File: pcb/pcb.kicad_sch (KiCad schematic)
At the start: 232 parts

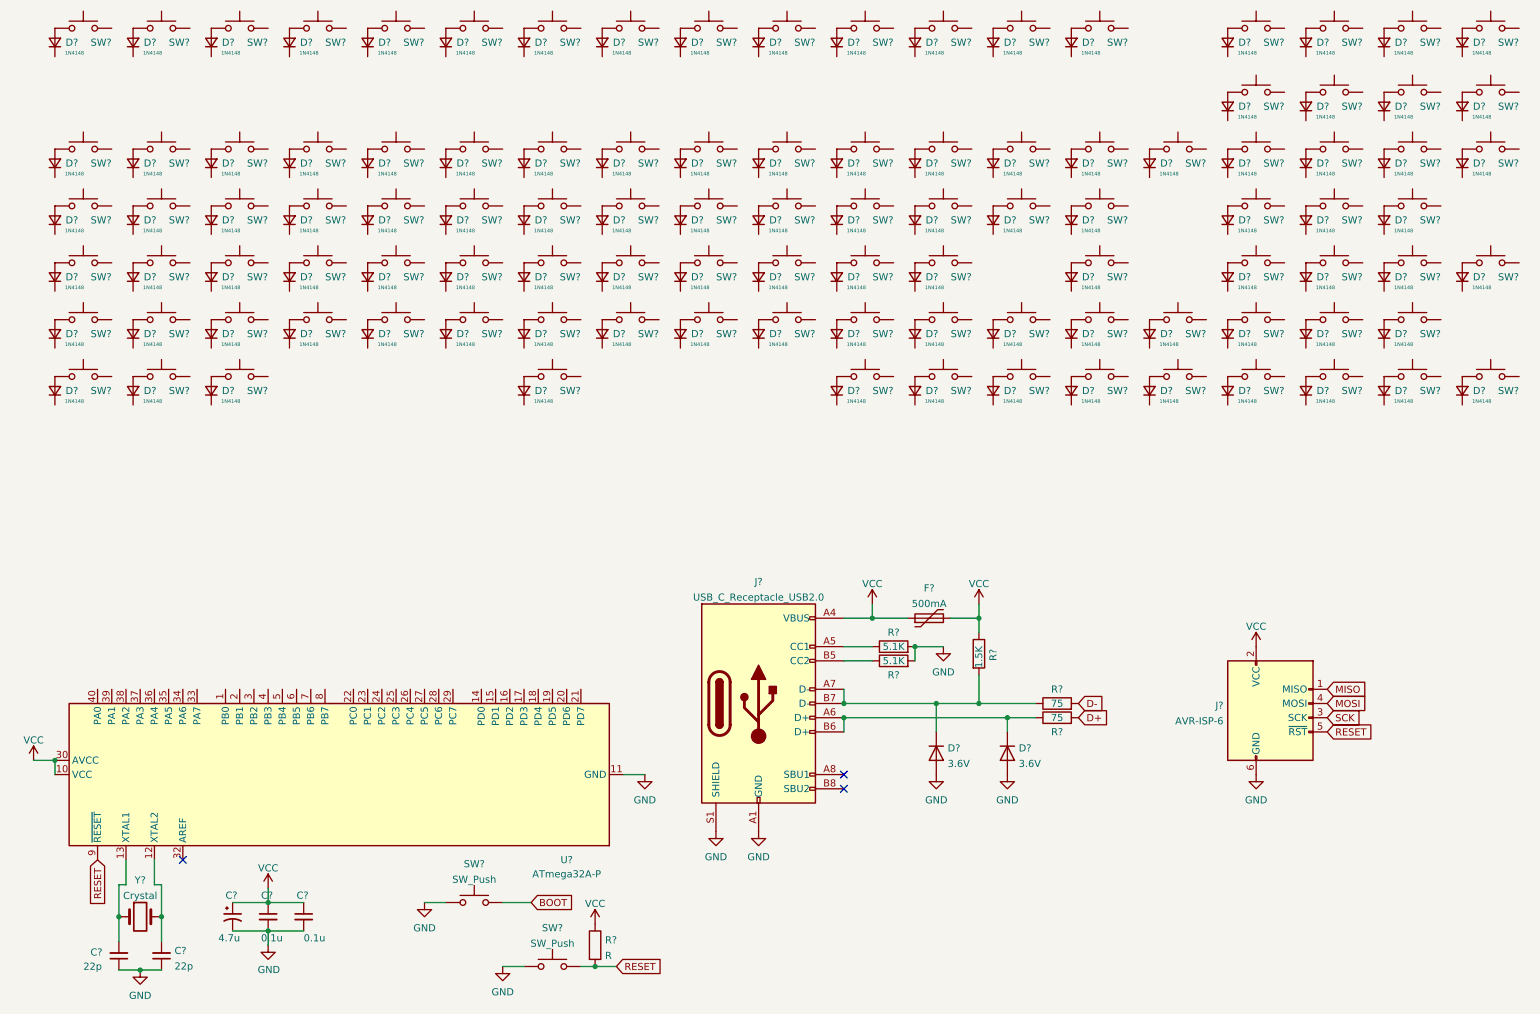
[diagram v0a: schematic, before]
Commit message: Wired duplex matrix
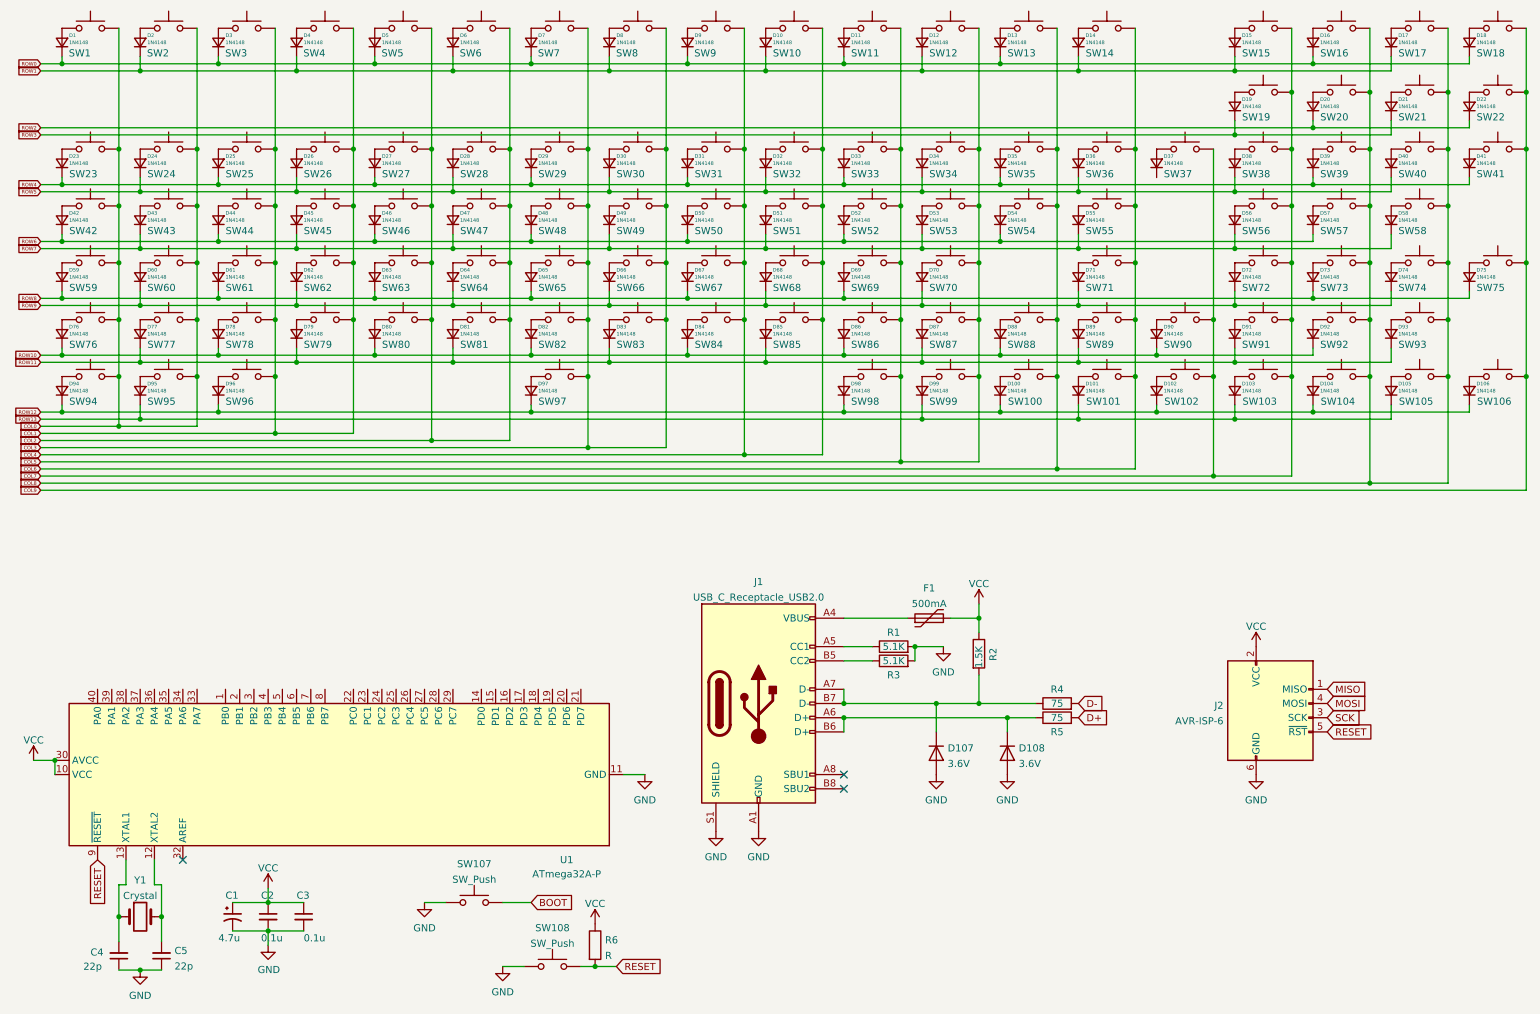
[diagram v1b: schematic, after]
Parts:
- gave numbers to parts that had none: 232
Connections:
- net VCC: no longer F1.1, J1.A4 (VBUS), J1.A9 (VBUS), J1.B4 (VBUS), J1.B9 (VBUS)
- net ROW3: now reaches D19.1 (K)
- net ROW3: now also D21.1 (K)
- net COL0: now reaches SW77.2
- net COL0: now also SW1.2, SW2.2, SW23.2, SW24.2, SW42.2, SW43.2, SW59.2, SW60.2, SW76.2, SW94.2, SW95.2
- net COL8: now reaches SW20.2
- net COL8: now also SW104.2, SW105.2, SW16.2, SW17.2, SW21.2, SW39.2, SW40.2, SW57.2, SW58.2, SW73.2, SW74.2, SW92.2, SW93.2
- net ROW9: now reaches D70.1 (K)
- net ROW9: now also D60.1 (K), D62.1 (K), D64.1 (K), D66.1 (K), D68.1 (K), D71.1 (K), D72.1 (K), D74.1 (K)
- net ROW1: now reaches D10.1 (K)
- net ROW1: now also D12.1 (K), D14.1 (K), D15.1 (K), D17.1 (K), D2.1 (K), D4.1 (K), D6.1 (K), D8.1 (K)
- net ROW8: now reaches D65.1 (K)
- net ROW8: now also D59.1 (K), D61.1 (K), D63.1 (K), D67.1 (K), D69.1 (K), D73.1 (K), D75.1 (K)
- net ROW7: now reaches D43.1 (K)
- net ROW7: now also D45.1 (K), D47.1 (K), D49.1 (K), D51.1 (K), D53.1 (K), D55.1 (K), D56.1 (K), D58.1 (K)
- net COL7: now reaches SW38.2
- net COL7: now also SW102.2, SW103.2, SW15.2, SW19.2, SW37.2, SW56.2, SW72.2, SW90.2, SW91.2
- net ROW12: now reaches D98.1 (K)
- net ROW12: now also D100.1 (K), D102.1 (K), D104.1 (K), D106.1 (K), D94.1 (K), D96.1 (K), D97.1 (K)
- net ROW5: now reaches D34.1 (K)
- net ROW5: now also D24.1 (K), D26.1 (K), D28.1 (K), D30.1 (K), D32.1 (K), D36.1 (K), D38.1 (K), D40.1 (K)
- net COL1: now reaches SW4.2
- net COL1: now also SW25.2, SW26.2, SW3.2, SW44.2, SW45.2, SW61.2, SW62.2, SW78.2, SW79.2, SW96.2
- net COL3: now reaches SW82.2
- net COL3: now also SW29.2, SW30.2, SW48.2, SW49.2, SW65.2, SW66.2, SW7.2, SW8.2, SW83.2, SW97.2
- net ROW11: now reaches D91.1 (K)
- net ROW11: now also D77.1 (K), D79.1 (K), D81.1 (K), D83.1 (K), D85.1 (K), D87.1 (K), D89.1 (K), D93.1 (K)
- net COL5: now reaches SW52.2
- net COL5: now also SW11.2, SW12.2, SW33.2, SW34.2, SW53.2, SW69.2, SW70.2, SW86.2, SW87.2, SW98.2, SW99.2
- net COL4: now reaches SW84.2
- net COL4: now also SW10.2, SW31.2, SW32.2, SW50.2, SW51.2, SW67.2, SW68.2, SW85.2, SW9.2
- net ROW0: now reaches D16.1 (K)
- net ROW0: now also D1.1 (K), D11.1 (K), D13.1 (K), D18.1 (K), D3.1 (K), D5.1 (K), D7.1 (K), D9.1 (K)
- net COL2: now reaches SW47.2
- net COL2: now also SW27.2, SW28.2, SW46.2, SW5.2, SW6.2, SW63.2, SW64.2, SW80.2, SW81.2
- net ROW10: now reaches D76.1 (K)
- net ROW10: now also D78.1 (K), D80.1 (K), D82.1 (K), D84.1 (K), D86.1 (K), D88.1 (K), D90.1 (K), D92.1 (K)
- net ROW4: now reaches D27.1 (K)
- net ROW4: now also D23.1 (K), D25.1 (K), D29.1 (K), D31.1 (K), D33.1 (K), D35.1 (K), D39.1 (K), D41.1 (K)
- net ROW13: now reaches D105.1 (K)
- net ROW13: now also D101.1 (K), D103.1 (K), D95.1 (K), D99.1 (K)
- net ROW2: now reaches D20.1 (K)
- net ROW2: now also D22.1 (K)
- net COL6: now reaches SW36.2
- net COL6: now also SW100.2, SW101.2, SW13.2, SW14.2, SW35.2, SW54.2, SW55.2, SW71.2, SW88.2, SW89.2
- net ROW6: now reaches D44.1 (K)
- net ROW6: now also D42.1 (K), D46.1 (K), D48.1 (K), D50.1 (K), D52.1 (K), D54.1 (K), D57.1 (K)
- net COL9: now reaches SW106.2
- net COL9: now also SW18.2, SW22.2, SW41.2, SW75.2
- new net: F1.1, J1.A4 (VBUS), J1.A9 (VBUS), J1.B4 (VBUS), J1.B9 (VBUS)
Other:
- moved on the sheet: D1, D10, D100, D101, D102, D103, D104, D105, D106, D11, D12, D13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

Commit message: Redid wiring on schematic because I hate myself
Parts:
- added SW107: 1U CTRL, MX_Only:MXOnly-1U-NoLED, symbol Switch:SW_Push
- added SW108, SW109, SW110, SW111, SW112, SW113: 1U, MX_Only:MXOnly-1U-NoLED, symbol Switch:SW_Push
- added SW114, SW119: 1.5U CTRL, MX_Only:MXOnly-1.5U-NoLED, symbol Switch:SW_Push
- added SW115: 1U GUI, MX_Only:MXOnly-1U-NoLED, symbol Switch:SW_Push
- added SW116, SW118: 1.5U ALT, MX_Only:MXOnly-1.5U-NoLED, symbol Switch:SW_Push
- added SW117: 7U SPACE, MX_Only:MXOnly-7U-NoLED, symbol Switch:SW_Push
- added SW120: 1.5U GUI, MX_Only:MXOnly-1.5U-NoLED, symbol Switch:SW_Push
- added SW121: 6U SPACE, MX_Only:MXOnly-6U-NoLED, symbol Switch:SW_Push
- C1: footprint cftkb:CP_Radial_D4.0mm_P1.50mm -> Capacitor_THT:CP_Radial_D4.0mm_P1.50mm
- C2, C3: footprint cftkb:C_Disc_D4.3mm_W1.9mm_P5.00mm -> Capacitor_THT:C_Disc_D4.3mm_W1.9mm_P5.00mm
- C4, C5: footprint (none) -> Capacitor_THT:C_Disc_D3.0mm_W1.6mm_P2.50mm
- D1, D10, D100, D101, D102, D103, D104, D105, D106, D11, D12, D13, D14, D15, D16, D17, D18, D19, D2, D20, D21, D22, D23, D24, D25, D26, D27, D28, D29, D3, D30, D31, D32, D33, D34, D35, D36, D37, D38, D39, D4, D40, D41, D42, D43, D44, D45, D46, D47, D48, D49, D5, D50, D51, D52, D53, D54, D55, D56, D57, D58, D59, D6, D60, D61, D62, D63, D64, D65, D66, D67, D68, D69, D7, D70, D71, D72, D73, D74, D75, D76, D77, D78, D79, D8, D80, D81, D82, D83, D84, D85, D86, D87, D88, D89, D9, D90, D91, D92, D93, D94, D95, D96, D97, D98, D99: footprint (none) -> Diode_THT:D_DO-35_SOD27_P7.62mm_Horizontal
- D107, D108: footprint (none) -> Diode_THT:D_DO-41_SOD81_P7.62mm_Horizontal
- F1: footprint (none) -> Fuse:Fuse_BelFuse_0ZRE0025FF_L9.6mm_W3.8mm
- J1: footprint (none) -> Connector_USB:USB_C_Receptacle_GCT_USB4085
- J2: footprint (none) -> Connector_PinHeader_2.54mm:PinHeader_2x03_P2.54mm_Vertical
- R1, R2, R3, R4, R5: footprint (none) -> Resistor_THT:R_Axial_DIN0204_L3.6mm_D1.6mm_P7.62mm_Horizontal
- R6: value R -> 10k; footprint (none) -> Resistor_THT:R_Axial_DIN0204_L3.6mm_D1.6mm_P7.62mm_Horizontal
- SW1, SW10, SW11, SW12, SW13, SW14, SW15, SW16, SW17, SW18, SW19, SW2, SW20, SW21, SW22, SW23, SW24, SW25, SW26, SW27, SW28, SW29, SW3, SW30, SW31, SW32, SW33, SW34, SW35, SW36, SW37, SW38, SW39, SW4, SW40, SW42, SW44, SW45, SW46, SW47, SW48, SW49, SW5, SW50, SW51, SW52, SW53, SW54, SW56, SW57, SW58, SW59, SW6, SW63, SW64, SW65, SW66, SW67, SW68, SW69, SW7, SW70, SW71, SW72, SW73, SW75, SW76, SW77, SW78, SW8, SW82, SW83, SW84, SW85, SW86, SW87, SW88, SW89, SW9, SW90, SW91, SW92, SW94, SW95, SW96, SW97, SW98: value SW_Push -> 1U; footprint (none) -> MX_Only:MXOnly-1U-NoLED
- SW100, SW41, SW60, SW74: value SW_Push -> 2U; footprint (none) -> MX_Only:MXOnly-2U-NoLED
- SW101: value SW_Push -> 1.25U CTRL; footprint (none) -> MX_Only:MXOnly-1.25U-NoLED
- SW102: value SW_Push -> 1.25U GUI; footprint (none) -> MX_Only:MXOnly-1.25U-NoLED
- SW103: value SW_Push -> 1.25U ALT; footprint (none) -> MX_Only:MXOnly-1.25U-NoLED
- SW104: value SW_Push -> 6.25u SPACE; footprint (none) -> MX_Only:MXOnly-6.25U-NoLED
- SW105: value SW_Push -> 1U ALT; footprint (none) -> MX_Only:MXOnly-1U-NoLED
- SW106: value SW_Push -> 1U GUI; footprint (none) -> MX_Only:MXOnly-1U-NoLED
- SW122: renamed from SW107; footprint (none) -> Button_Switch_THT:SW_PUSH_6mm_H5mm
- SW123: renamed from SW108; footprint (none) -> Button_Switch_THT:SW_PUSH_6mm_H5mm
- SW43, SW55: value SW_Push -> 1.5U; footprint (none) -> MX_Only:MXOnly-1.5U-NoLED
- SW61: value SW_Push -> ISO ENTER; footprint (none) -> MX_Only:MXOnly-ISO-NoLED
- SW62: value SW_Push -> CAPSLOCK; footprint (none) -> MX_Only:MXOnly-1.75U-NoLED
- SW79: value SW_Push -> STEPPED; footprint (none) -> MX_Only:MXOnly-1.25U-NoLED
- SW80: value SW_Push -> ISO 1U; footprint (none) -> MX_Only:MXOnly-1U-NoLED
- SW81: value SW_Push -> 2.25U; footprint (none) -> MX_Only:MXOnly-2.25U-NoLED
- SW93: value SW_Push -> 1.75U SHIFT; footprint (none) -> MX_Only:MXOnly-1.75U-NoLED
- SW99: value SW_Push -> ISO SHIFT; footprint (none) -> MX_Only:MXOnly-1.25U-NoLED
- Y1: footprint (none) -> Crystal:Crystal_HC49-4H_Vertical
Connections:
- net COL0: no longer SW1.2, SW2.2, SW23.2, SW24.2, SW42.2, SW43.2, SW59.2, SW60.2, SW76.2, SW77.2, SW94.2, SW95.2
- net COL1: no longer SW25.2, SW26.2, SW3.2, SW4.2, SW44.2, SW45.2, SW61.2, SW62.2, SW78.2, SW79.2, SW96.2
- net COL2: no longer SW27.2, SW28.2, SW46.2, SW47.2, SW5.2, SW6.2, SW63.2, SW64.2, SW80.2, SW81.2
- net COL3: no longer SW29.2, SW30.2, SW48.2, SW49.2, SW65.2, SW66.2, SW7.2, SW8.2, SW82.2, SW83.2, SW97.2
- net COL4: no longer SW10.2, SW31.2, SW32.2, SW50.2, SW51.2, SW67.2, SW68.2, SW84.2, SW85.2, SW9.2
- net COL5: no longer SW11.2, SW12.2, SW33.2, SW34.2, SW52.2, SW53.2, SW69.2, SW70.2, SW86.2, SW87.2, SW98.2, SW99.2
- net COL6: no longer SW100.2, SW101.2, SW13.2, SW14.2, SW35.2, SW36.2, SW54.2, SW55.2, SW71.2, SW88.2, SW89.2
- net COL7: no longer SW102.2, SW103.2, SW15.2, SW19.2, SW37.2, SW38.2, SW56.2, SW72.2, SW90.2, SW91.2
- net COL8: no longer SW104.2, SW105.2, SW16.2, SW17.2, SW20.2, SW21.2, SW39.2, SW40.2, SW57.2, SW58.2, SW73.2, SW74.2, SW92.2, SW93.2
- net COL9: no longer SW106.2, SW18.2, SW22.2, SW41.2, SW75.2
- net ROW0: no longer D1.1 (K), D11.1 (K), D13.1 (K), D16.1 (K), D18.1 (K), D3.1 (K), D5.1 (K), D7.1 (K), D9.1 (K)
- net ROW1: no longer D10.1 (K), D12.1 (K), D14.1 (K), D15.1 (K), D17.1 (K), D2.1 (K), D4.1 (K), D6.1 (K), D8.1 (K)
- net ROW10: no longer D76.1 (K), D78.1 (K), D80.1 (K), D82.1 (K), D84.1 (K), D86.1 (K), D88.1 (K), D90.1 (K), D92.1 (K)
- net ROW11: no longer D77.1 (K), D79.1 (K), D81.1 (K), D83.1 (K), D85.1 (K), D87.1 (K), D89.1 (K), D91.1 (K), D93.1 (K)
- net ROW12: no longer D100.1 (K), D102.1 (K), D104.1 (K), D106.1 (K), D94.1 (K), D96.1 (K), D97.1 (K), D98.1 (K)
- net ROW13: no longer D101.1 (K), D103.1 (K), D105.1 (K), D95.1 (K), D99.1 (K)
- net ROW2: no longer D20.1 (K), D22.1 (K)
- net ROW3: no longer D19.1 (K), D21.1 (K)
- net ROW4: no longer D23.1 (K), D25.1 (K), D27.1 (K), D29.1 (K), D31.1 (K), D33.1 (K), D35.1 (K), D39.1 (K), D41.1 (K)
- net ROW5: no longer D24.1 (K), D26.1 (K), D28.1 (K), D30.1 (K), D32.1 (K), D34.1 (K), D36.1 (K), D38.1 (K), D40.1 (K)
- net ROW6: no longer D42.1 (K), D44.1 (K), D46.1 (K), D48.1 (K), D50.1 (K), D52.1 (K), D54.1 (K), D57.1 (K)
- net ROW7: no longer D43.1 (K), D45.1 (K), D47.1 (K), D49.1 (K), D51.1 (K), D53.1 (K), D55.1 (K), D56.1 (K), D58.1 (K)
- net ROW8: no longer D59.1 (K), D61.1 (K), D63.1 (K), D65.1 (K), D67.1 (K), D69.1 (K), D73.1 (K), D75.1 (K)
- net ROW9: no longer D60.1 (K), D62.1 (K), D64.1 (K), D66.1 (K), D68.1 (K), D70.1 (K), D71.1 (K), D72.1 (K), D74.1 (K)
- net at D77.2 (A): now also SW82.1; no longer SW77.1
- net at SW70.1: now also D67.2 (A); no longer D70.2 (A)
- net at SW65.1: now also D62.2 (A); no longer D65.2 (A)
- net at D43.2 (A): now also SW44.1; no longer SW43.1
- net at SW98.1: now also D93.2 (A), SW100.1; no longer D98.2 (A)
- net at D95.2 (A): now also SW102.1, SW115.1, SW120.1; no longer SW95.1
- net at SW74.1: now also D71.2 (A), SW61.1; no longer D74.2 (A)
- net at D82.2 (A): now also SW87.1; no longer SW82.1
- net at D45.2 (A): now also SW46.1; no longer SW45.1
- net at D91.2 (A): now also SW96.1; no longer SW91.1
- net at SW66.1: now also D63.2 (A); no longer D66.2 (A)
- net at D56.2 (A): now also SW57.1; no longer SW56.1
- net at SW52.1: now also D51.2 (A); no longer D52.2 (A)
- net at SW84.1: now also D79.2 (A); no longer D84.2 (A)
- net at SW92.1: now also D87.2 (A); no longer D92.2 (A)
- net at SW79.1: now also D59.2 (A), SW62.1; no longer D79.2 (A)
- net at SW94.1: now also D89.2 (A); no longer D94.2 (A)
- net at D69.2 (A): now also SW72.1; no longer SW69.1
- net at SW47.1: now also D46.2 (A); no longer D47.2 (A)
- net at D76.2 (A): now also SW81.1, SW99.1; no longer SW76.1
- net at SW60.1: now also D58.2 (A), SW59.1; no longer D60.2 (A)
- net at D96.2 (A): now also SW103.1, SW116.1; no longer SW96.1
- net at D72.2 (A): now also SW75.1; no longer SW72.1
- net at D99.2 (A): now also SW106.1; no longer SW99.1
- net at D73.2 (A): now also SW76.1; no longer SW73.1
- net at D105.2 (A): now also SW112.1; no longer SW105.1
- net at SW88.1: now also D83.2 (A); no longer D88.2 (A)
- net at SW78.1: now also D75.2 (A); no longer D78.2 (A)
- net at SW68.1: now also D65.2 (A); no longer D68.2 (A)
- net at SW89.1: now also D84.2 (A); no longer D89.2 (A)
- net at SW93.1: now also D88.2 (A); no longer D93.2 (A)
- net at D49.2 (A): now also SW50.1; no longer SW49.1
- net at D61.2 (A): now also SW64.1; no longer SW61.1
- net at SW71.1: now also D68.2 (A); no longer D71.2 (A)
- net at SW101.1: now also D94.2 (A), SW114.1; no longer D101.2 (A)
- net at D81.2 (A): now also SW86.1; no longer SW81.1
- net at SW63.1: now also D60.2 (A); no longer D63.2 (A)
- net at D100.2 (A): now also SW107.1, SW119.1; no longer SW100.1
- net at SW90.1: now also D85.2 (A); no longer D90.2 (A)
- net at SW48.1: now also D47.2 (A); no longer D48.2 (A)
- net at D102.2 (A): now also SW109.1; no longer SW102.1
- net at SW80.1: now also D54.2 (A), SW55.1; no longer D80.2 (A)
- net at SW85.1: now also D80.2 (A); no longer D85.2 (A)
- net at D44.2 (A): now also SW45.1; no longer SW44.1
- net at SW54.1: now also D53.2 (A); no longer D54.2 (A)
- net at SW83.1: now also D78.2 (A); no longer D83.2 (A)
- net at SW42.1: now also D41.2 (A), SW41.2; no longer D42.2 (A)
- net at D55.2 (A): now also SW56.1; no longer SW55.1
- net at SW51.1: now also D50.2 (A); no longer D51.2 (A)
- net at SW58.1: now also D57.2 (A); no longer D58.2 (A)
- net at D86.2 (A): now also SW91.1; no longer SW86.1
- net at D103.2 (A): now also SW110.1; no longer SW103.1
- net at SW67.1: now also D64.2 (A); no longer D67.2 (A)
- net at SW53.1: now also D52.2 (A); no longer D53.2 (A)
- net at D97.2 (A): now also SW104.1, SW117.1, SW121.1; no longer SW97.1
- net at D37.1 (K): now also D24.1 (K), D26.1 (K), D28.1 (K), D30.1 (K), D32.1 (K), D34.1 (K), D39.1 (K), D41.1 (K)
- net at D106.2 (A): now also SW113.1; no longer SW106.1
- net at SW41.1: now also SW42.2; no longer D41.2 (A)
- net at D104.2 (A): now also SW111.1; no longer SW104.1
- new net: D1.1 (K), D11.1 (K), D13.1 (K), D16.1 (K), D18.1 (K), D3.1 (K), D5.1 (K), D7.1 (K), D9.1 (K)
- new net: SW100.2, SW98.2
- new net: D76.1 (K), D78.1 (K), D80.1 (K), D82.1 (K), D84.1 (K), D86.1 (K), D88.1 (K), D89.1 (K), D91.1 (K), D93.1 (K)
- new net: D23.1 (K), D25.1 (K), D27.1 (K), D29.1 (K), D31.1 (K), D33.1 (K), D35.1 (K), D36.1 (K), D38.1 (K), D40.1 (K)
- new net: SW61.2, SW74.2
- new net: D77.1 (K), D79.1 (K), D81.1 (K), D83.1 (K), D85.1 (K), D87.1 (K), D90.1 (K), D92.1 (K)
- new net: SW59.2, SW60.2
- new net: D101.1 (K), D103.1 (K), D105.1 (K), D95.1 (K), D99.1 (K)
- new net: D42.1 (K), D44.1 (K), D46.1 (K), D48.1 (K), D50.1 (K), D52.1 (K), D54.1 (K), D56.1 (K), D58.1 (K)
- new net: D100.1 (K), D102.1 (K), D104.1 (K), D106.1 (K), D94.1 (K), D96.1 (K), D97.1 (K), D98.1 (K)
- new net: SW62.2, SW79.2
- new net: D10.1 (K), D12.1 (K), D14.1 (K), D15.1 (K), D17.1 (K), D2.1 (K), D4.1 (K), D6.1 (K), D8.1 (K)
- new net: SW81.2, SW99.2
- new net: D19.1 (K), D21.1 (K)
- new net: D59.1 (K), D61.1 (K), D63.1 (K), D65.1 (K), D67.1 (K), D69.1 (K), D71.1 (K), D73.1 (K), D75.1 (K)
- new net: D20.1 (K), D22.1 (K)
- new net: SW107.2, SW119.2
- new net: D60.1 (K), D62.1 (K), D64.1 (K), D66.1 (K), D68.1 (K), D70.1 (K), D72.1 (K), D74.1 (K)
- new net: D70.2 (A), SW73.1
- new net: SW55.2, SW80.2
- new net: D43.1 (K), D45.1 (K), D47.1 (K), D49.1 (K), D51.1 (K), D53.1 (K), D55.1 (K), D57.1 (K)
- new net: D92.2 (A), SW97.1
- new net: D90.2 (A), SW95.1
- new net: D42.2 (A), SW43.1
- new net: D74.2 (A), SW77.1
- new net: D101.2 (A), SW108.1
- new net: D98.2 (A), SW105.1, SW118.1
- new net: D66.2 (A), SW69.1
- new net: D48.2 (A), SW49.1
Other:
- moved on the sheet: C1, C2, C3, C4, C5, D107, D108, F1, J1, J2, R1, R2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
